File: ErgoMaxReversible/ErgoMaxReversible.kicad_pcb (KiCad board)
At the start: 2 copper layers, 182.8 x 169.2 mm, 102 parts, among them J1 PJ-320A, K1 KEYSW, K10 KEYSW, K11 KEYSW, K12 KEYSW, K13 KEYSW, K14 KEYSW, K15 KEYSW, K16 KEYSW, K17 KEYSW, K18 KEYSW, K19 KEYSW, K2 KEYSW, K20 KEYSW, K21 KEYSW, K22 KEYSW, K23 KEYSW, K24 KEYSW, K25 KEYSW, K26 KEYSW, K27 KEYSW, K28 KEYSW, K29 KEYSW, K3 KEYSW, K30 KEYSW, K31 KEYSW, K32 KEYSW, K33 KEYSW, K34 KEYSW, K35 KEYSW, K36 KEYSW, K37 KEYSW, K38 KEYSW, K39 KEYSW, K4 KEYSW, K40 KEYSW, K41 KEYSW, K42 KEYSW, K43 KEYSW, K44 KEYSW, K5 KEYSW, K6 KEYSW, K7 KEYSW, K8 KEYSW, K9 KEYSW, U1 ProMicro

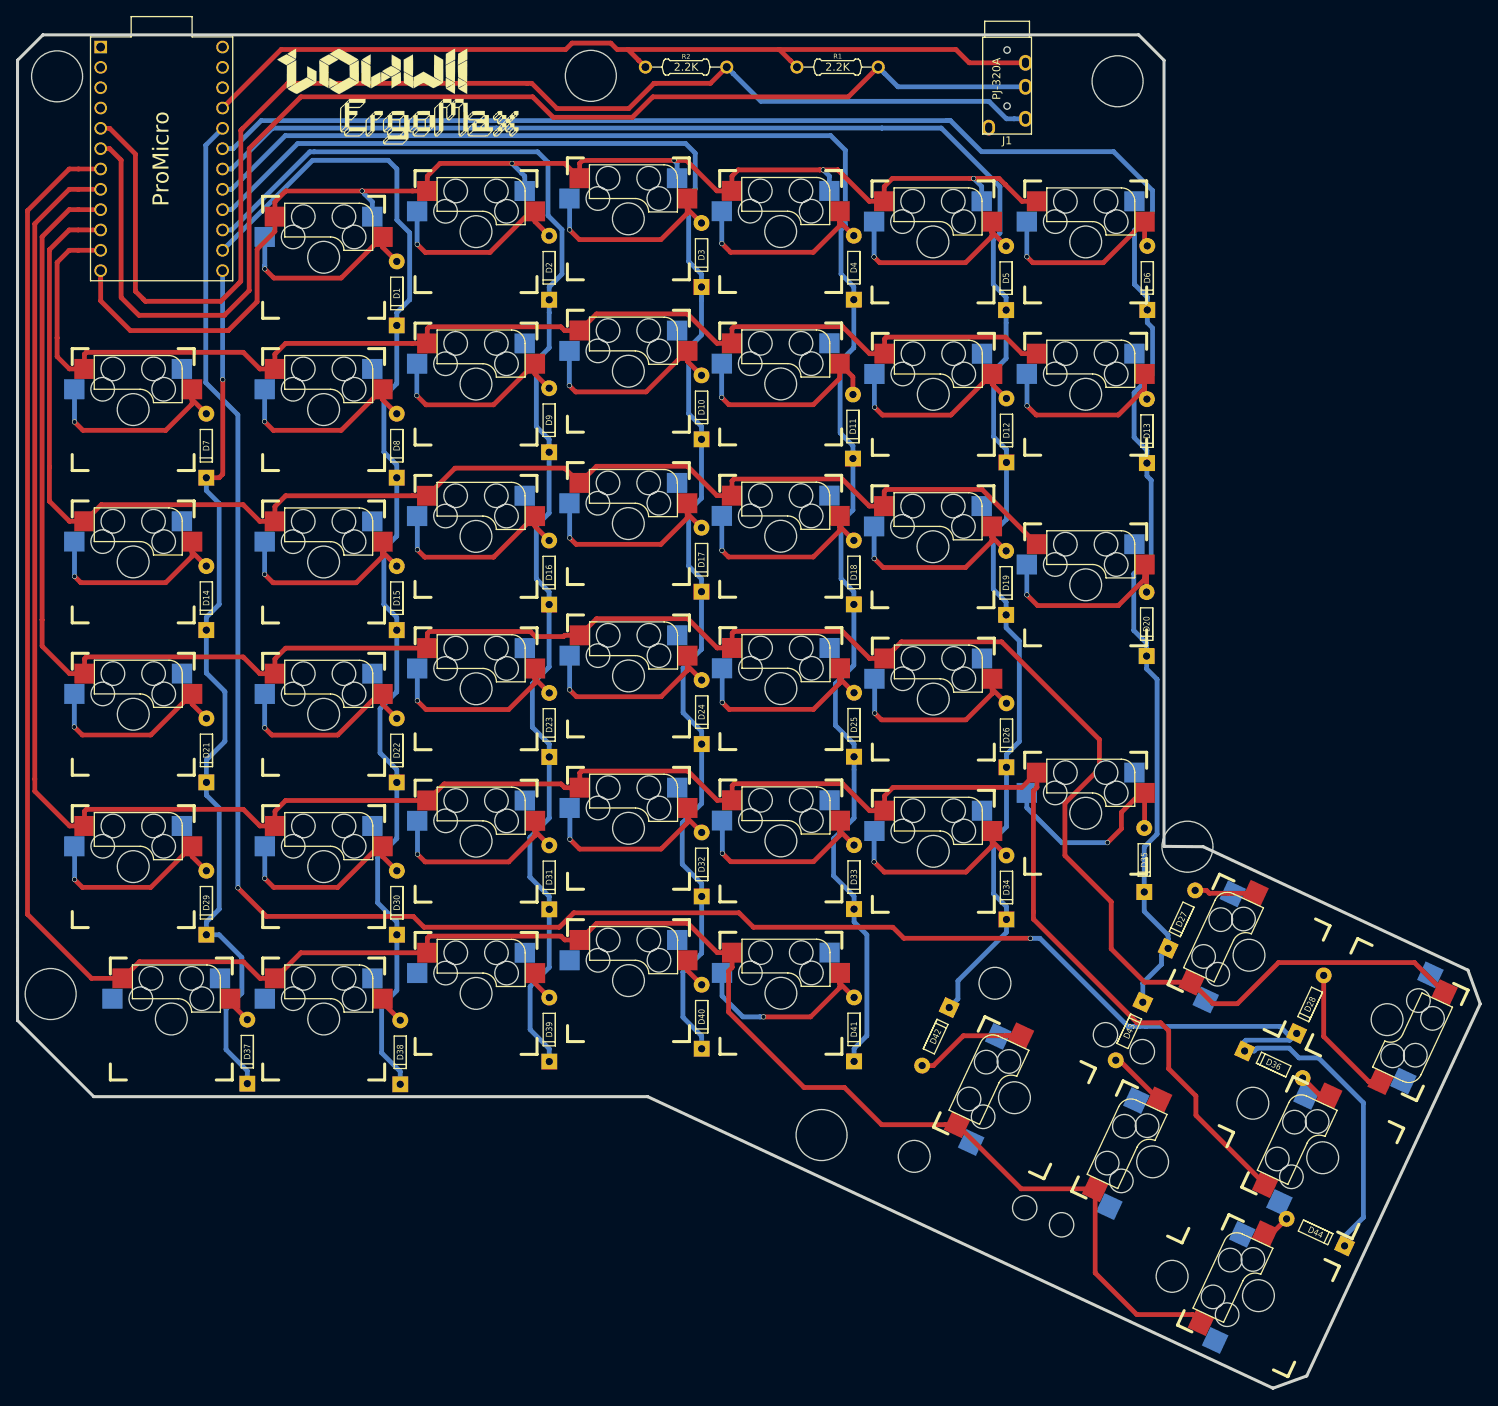
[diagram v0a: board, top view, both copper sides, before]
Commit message: more wiring on reversible PCB
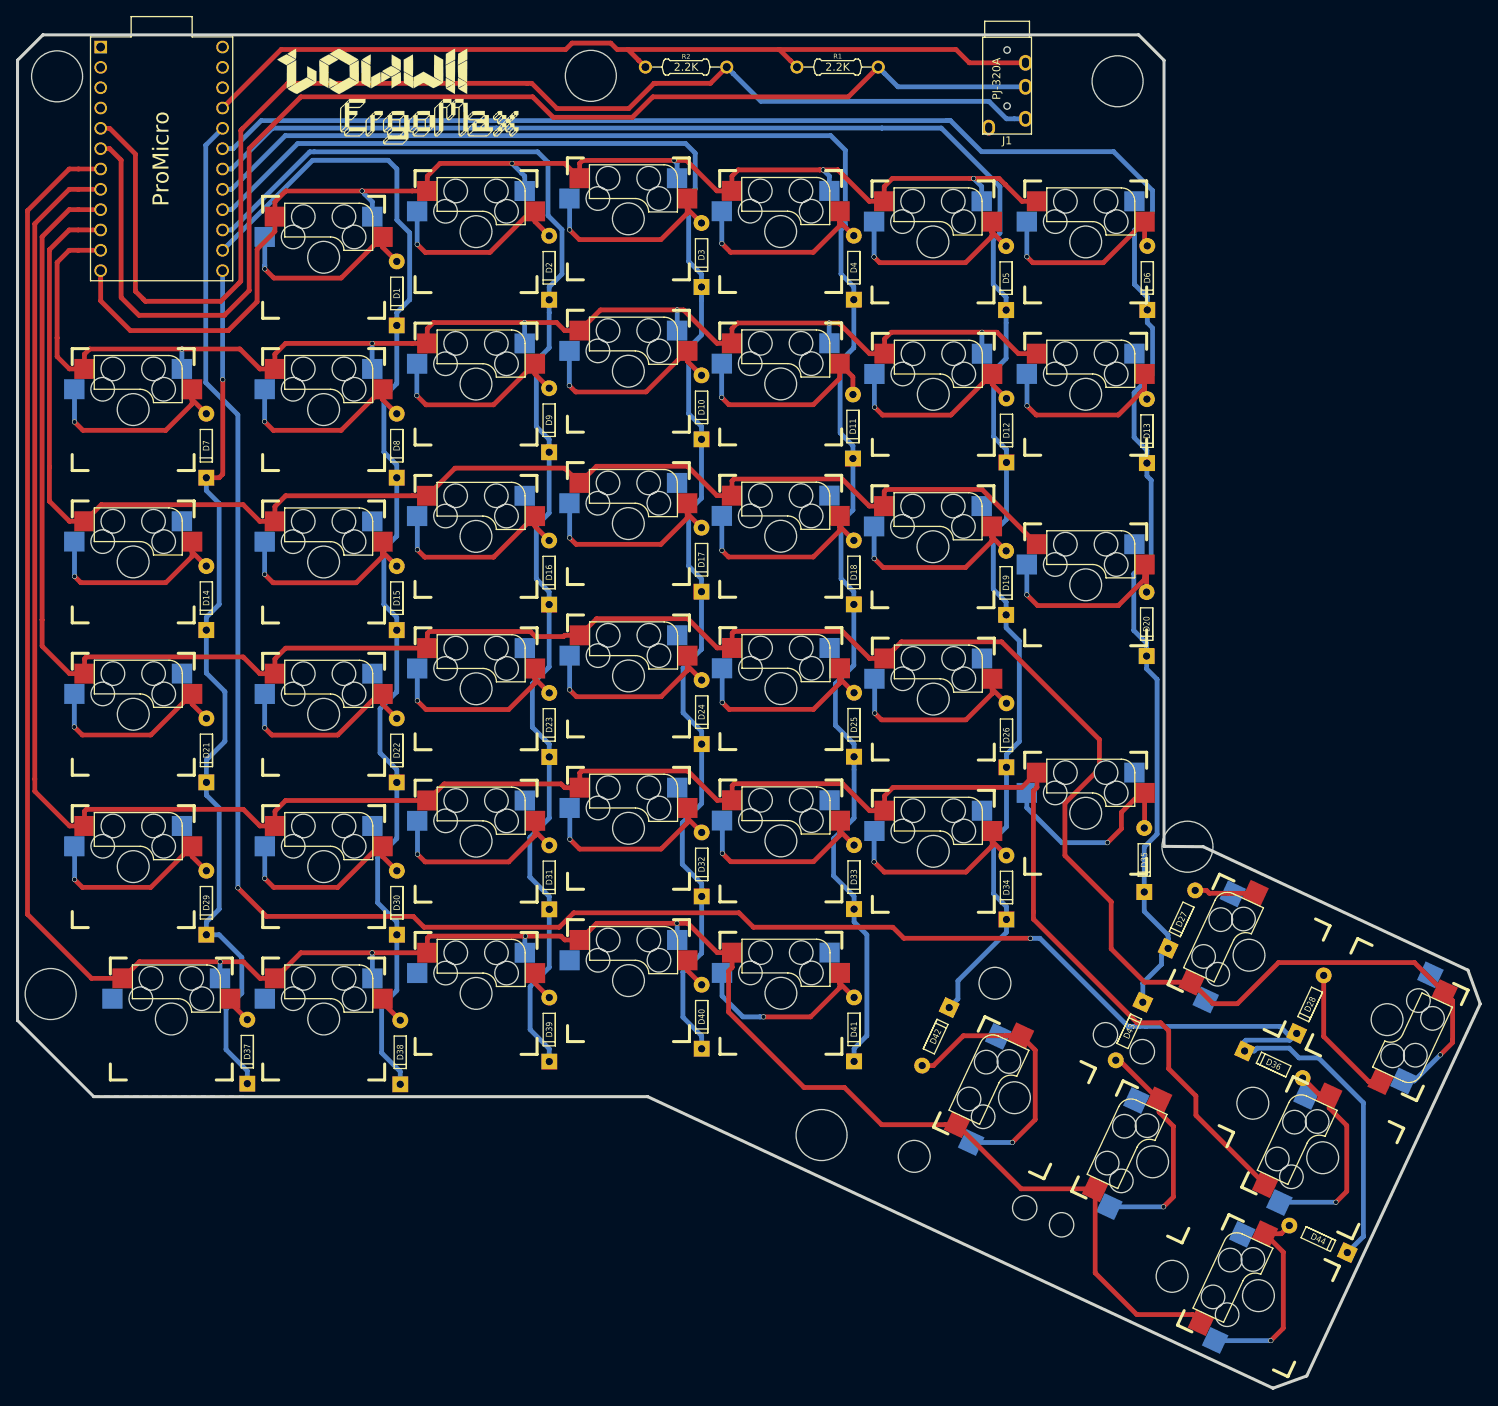
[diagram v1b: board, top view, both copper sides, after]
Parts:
- moved D44 0.90 mm to (272.9, 186.4)
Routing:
- net Net-(D44-Pad2): track 3.48 -> 26.3 mm, vias 0 -> 1
- net Net-(D36-Pad2): track 4.23 -> 26.1 mm, vias 0 -> 1
- net Net-(D43-Pad2): track 7.47 -> 28.9 mm, vias 0 -> 1
- net Net-(D42-Pad2): track 15.8 -> 36.2 mm, vias 0 -> 1
- net /Row1: track 156.9 -> 175.1 mm, vias 0 -> 6
- net /Row3: track 291.2 -> 306.0 mm, vias 0 -> 1
- net /Row5: track 287.2 -> 296.7 mm, vias 0 -> 4
- net /Col7: track 283.7 -> 284.4 mm

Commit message: wiring again for reversible pcb
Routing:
- net /Row2: track 180.2 -> 201.5 mm, vias 0 -> 6
- net /Row3: track 306.0 -> 324.1 mm, vias 1 -> 7

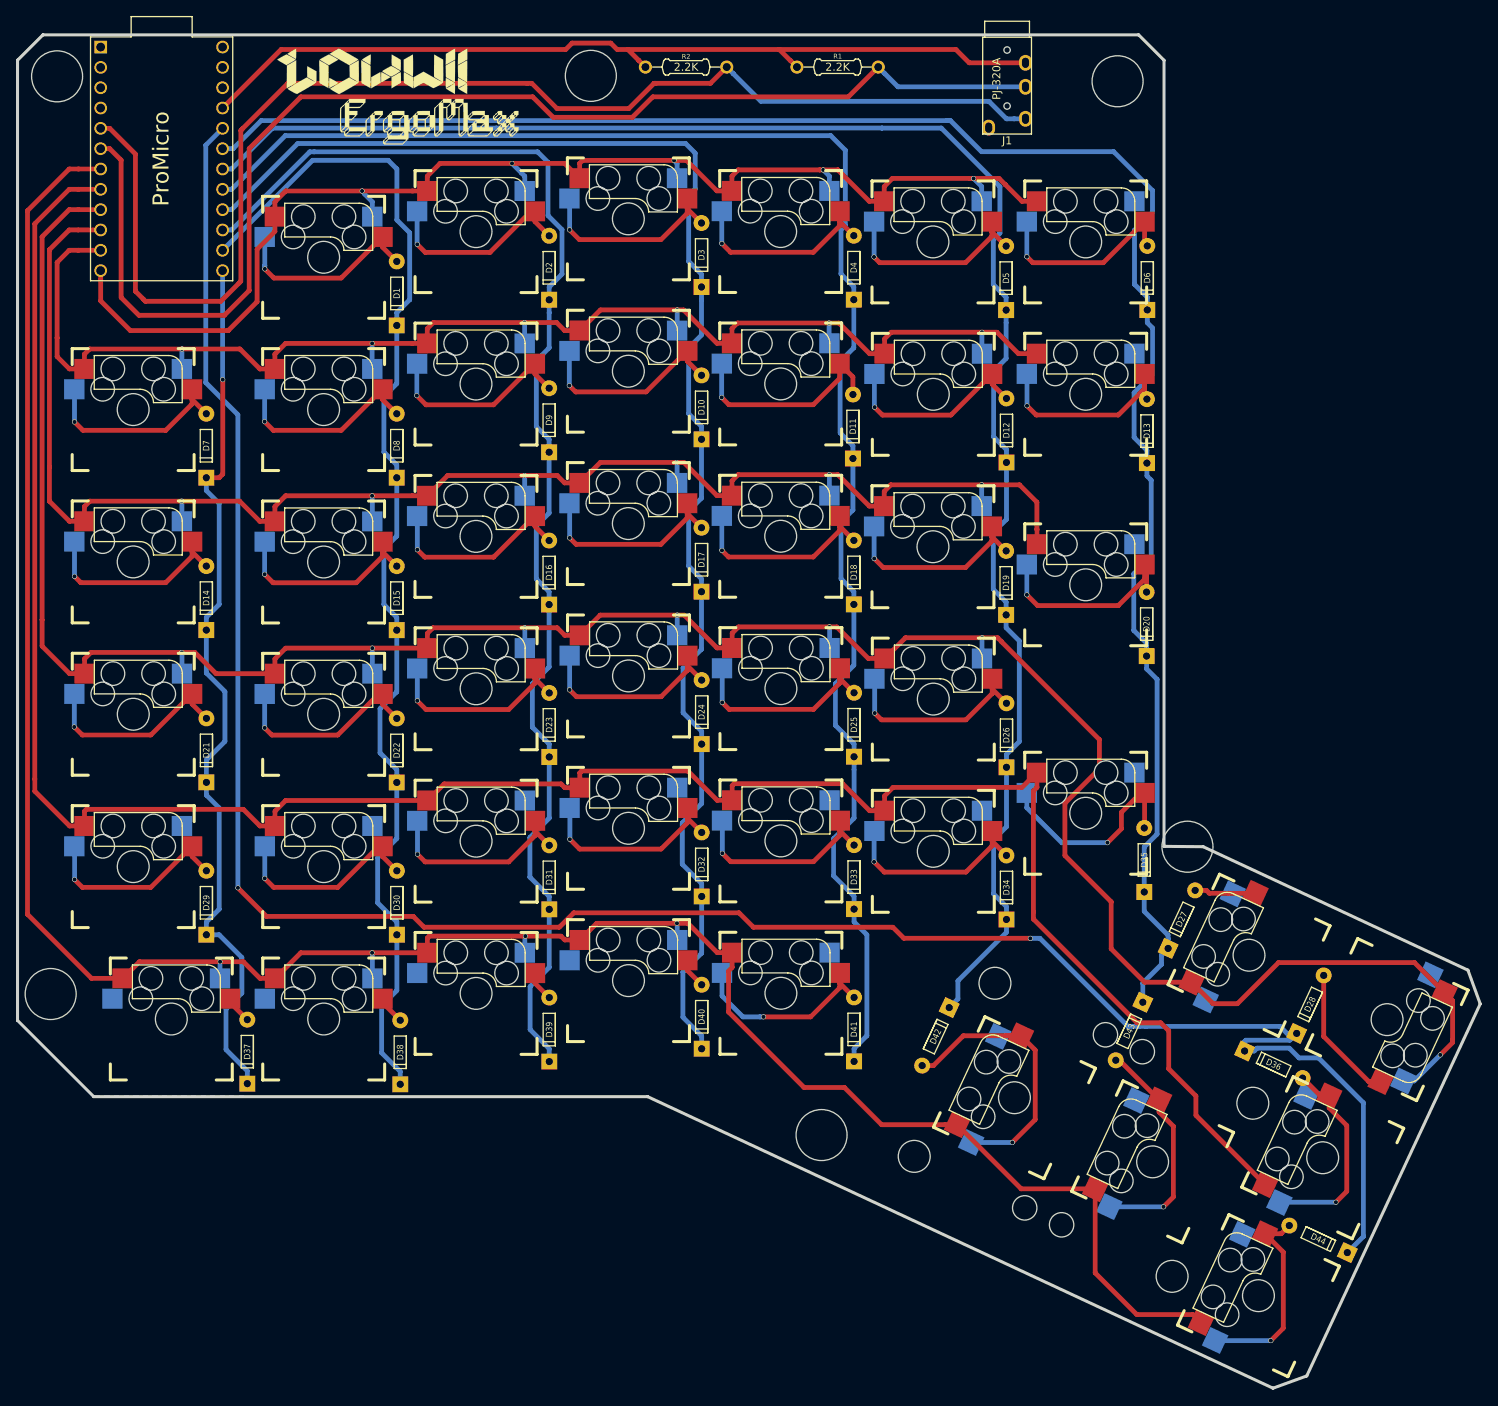
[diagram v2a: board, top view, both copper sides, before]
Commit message: improve wiring on reversible pcb
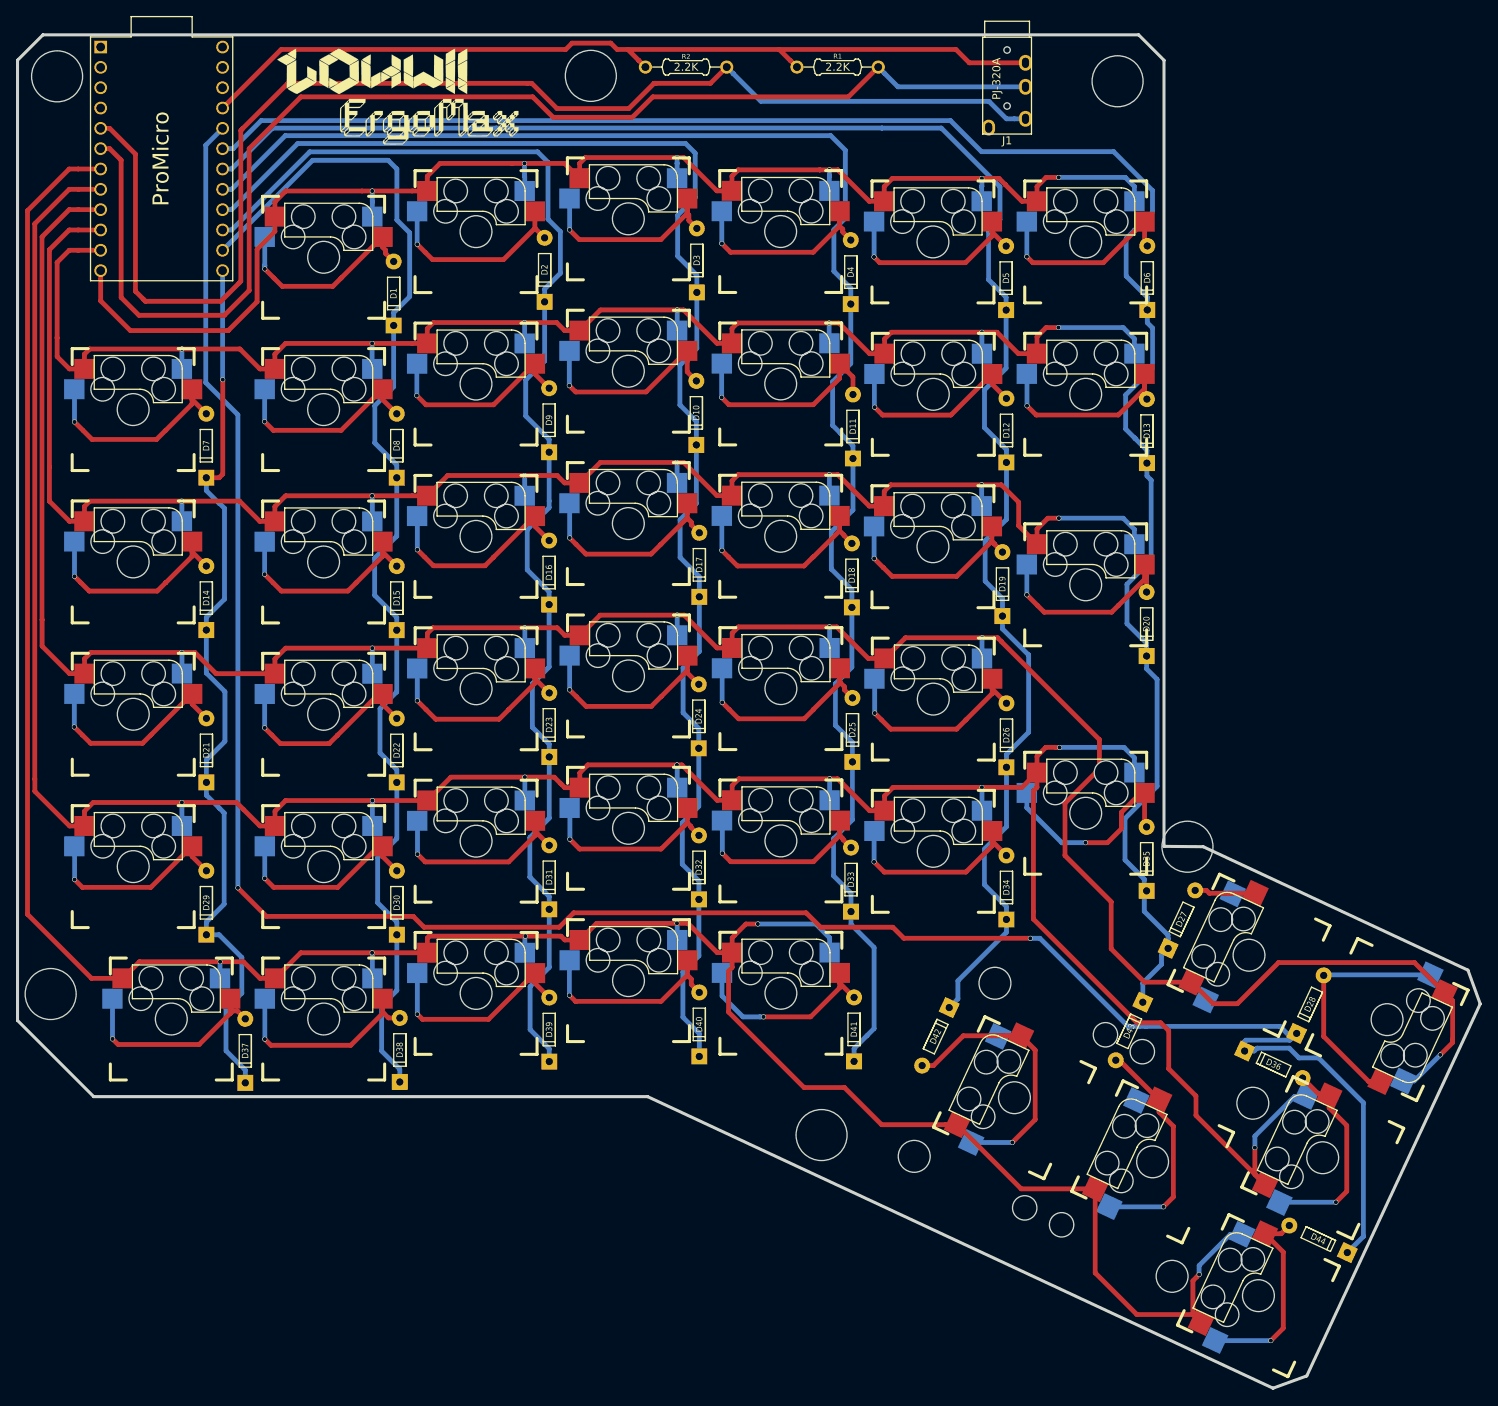
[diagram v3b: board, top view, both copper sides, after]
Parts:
- moved D40 1.00 mm to (195.6, 159.5)
- moved D10 0.95 mm to (195.2, 83.1)
- moved D3 0.89 mm to (195.3, 64.0)
- moved D17 0.69 mm to (195.6, 102.1)
- moved D25 0.67 mm to (214.7, 122.7)
- moved D4 0.67 mm to (214.5, 65.5)
- moved D24 0.64 mm to (195.5, 121.0)
- moved D2 0.62 mm to (176.2, 65.2)
- moved D32 0.50 mm to (195.5, 139.9)
- moved D33 0.49 mm to (214.5, 141.4)
- moved D19 0.48 mm to (233.5, 104.5)
- moved D18 0.45 mm to (214.6, 103.4)
- moved D1 0.39 mm to (157.4, 68.2)
- moved D35 0.32 mm to (251.5, 138.9)
- moved D38 0.30 mm to (158.1, 162.7)
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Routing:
- net /Row4: track 289.6 -> 341.9 mm, vias 0 -> 8
- net /Row5: track 296.7 -> 327.4 mm, vias 4 -> 6
- net Net-(D40-Pad2): track 3.80 -> 26.7 mm, vias 0 -> 1
- net Net-(D37-Pad2): track 3.51 -> 26.4 mm, vias 0 -> 1
- net Net-(D38-Pad2): track 3.62 -> 26.5 mm, vias 0 -> 1
- net Net-(D39-Pad2): track 3.80 -> 26.3 mm, vias 0 -> 1
- net /Row1: track 175.1 -> 192.3 mm, vias 6 -> 7
- net /Row2: track 201.5 -> 217.2 mm, vias 6 -> 7
- net /Row0: track 166.1 -> 181.5 mm, vias 5 -> 6
- net Net-(D28-Pad2): track 17.1 -> 30.5 mm
- net /Col6: track 232.1 -> 236.8 mm
- net /Col5: track 214.3 -> 218.5 mm
- net Net-(D25-Pad2): track 26.3 -> 29.2 mm
- net /Col4: track 204.2 -> 207.0 mm
- net /Col3: track 184.5 -> 186.4 mm
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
